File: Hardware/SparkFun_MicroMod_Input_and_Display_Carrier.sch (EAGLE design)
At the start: 64 parts, among them J1 MICROMOD-2222-C, J2 MICRO-SD, J3 USB-C_Prog, J4 AVR_SPI_PROG_3X2TESTPOINTS, J5 2.4" TFT, J6 QWIIC_RA, J7 CORTEX_JTAG_DEBUG, Q1 1.1A/60V/600mΩ, U2 ATTINY84, U5 AP7361C-33FGE

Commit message: QC Fixes
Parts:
- added TP1: TEST-POINT3, SparkFun-Connectors:TEST-POINT3
- J1: SPICEPREFIX (none) -> X
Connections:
- net SWDCK: now also TP1.1
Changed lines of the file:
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@@
 <layer number="255" name="routoute" color="7" fill="1" visible="no" active="no"/>
 </layers>
-<schematic xreflabel="%F%N/%S" xrefpart="/%S.%C%R">
+<schematic xreflabel="%F%N/%S" xrefpart="1_/%S.%C%R">
 <attributes>
 </attributes>
@@
 </classes>
 <parts>
-<part name="J1" library="SparkFun-MicroMod" deviceset="MICROMOD" device="-2222-C"/>
+<part name="J1" library="SparkFun-MicroMod" deviceset="MICROMOD" device="-2222-C">
+<attribute name="SPICEPREFIX" value="X"/>
+</part>
 <part name="J2" library="SparkFun-Connectors" deviceset="MICRO-SD-SPI" device="PUSH-PUSH" value="MICRO-SD"/>
 <part name="S1" library="SparkFun-Switches" deviceset="MOMENTARY-SWITCH-SPST" device="-SMD-5.2-TALL-REDUNDANT" value="Reset"/>
@@
 <part name="R9" library="SparkFun-Resistors" deviceset="10KOHM" device="-0603-1/10W-1%" value="10k"/>
 <part name="GND34" library="SparkFun-PowerSymbols" deviceset="GND" device=""/>
+<part name="TP1" library="SparkFun-Connectors" deviceset="TEST-POINT" device="3" value=""/>
 </parts>
 <sheets>
@@
 <attribute name="VALUE" x="15.24" y="22.606" size="1.778" layer="96" font="vector" align="top-center"/>
 </instance>
+<instance part="TP1" gate="G$1" x="185.42" y="40.64" smashed="yes">
+<attribute name="NAME" x="189.484" y="39.878" size="1.778" layer="95" font="vector"/>
+<attribute name="VALUE" x="182.88" y="38.1" size="1.778" layer="96" font="vector"/>
+</instance>
 </instances>
 <busses>
@@
 <label x="182.88" y="121.92" size="1.27" layer="95" font="vector" rot="R180" xref="yes"/>
 </segment>
-</net>
+<segment>
+<pinref part="TP1" gate="G$1" pin="1"/>
+<wire x1="185.42" y1="40.64" x2="182.88" y2="40.64" width="0.1524" layer="91"/>
+<label x="182.88" y="40.64" size="1.27" layer="95" rot="R180" xref="yes"/>
+</segment>
+</net>

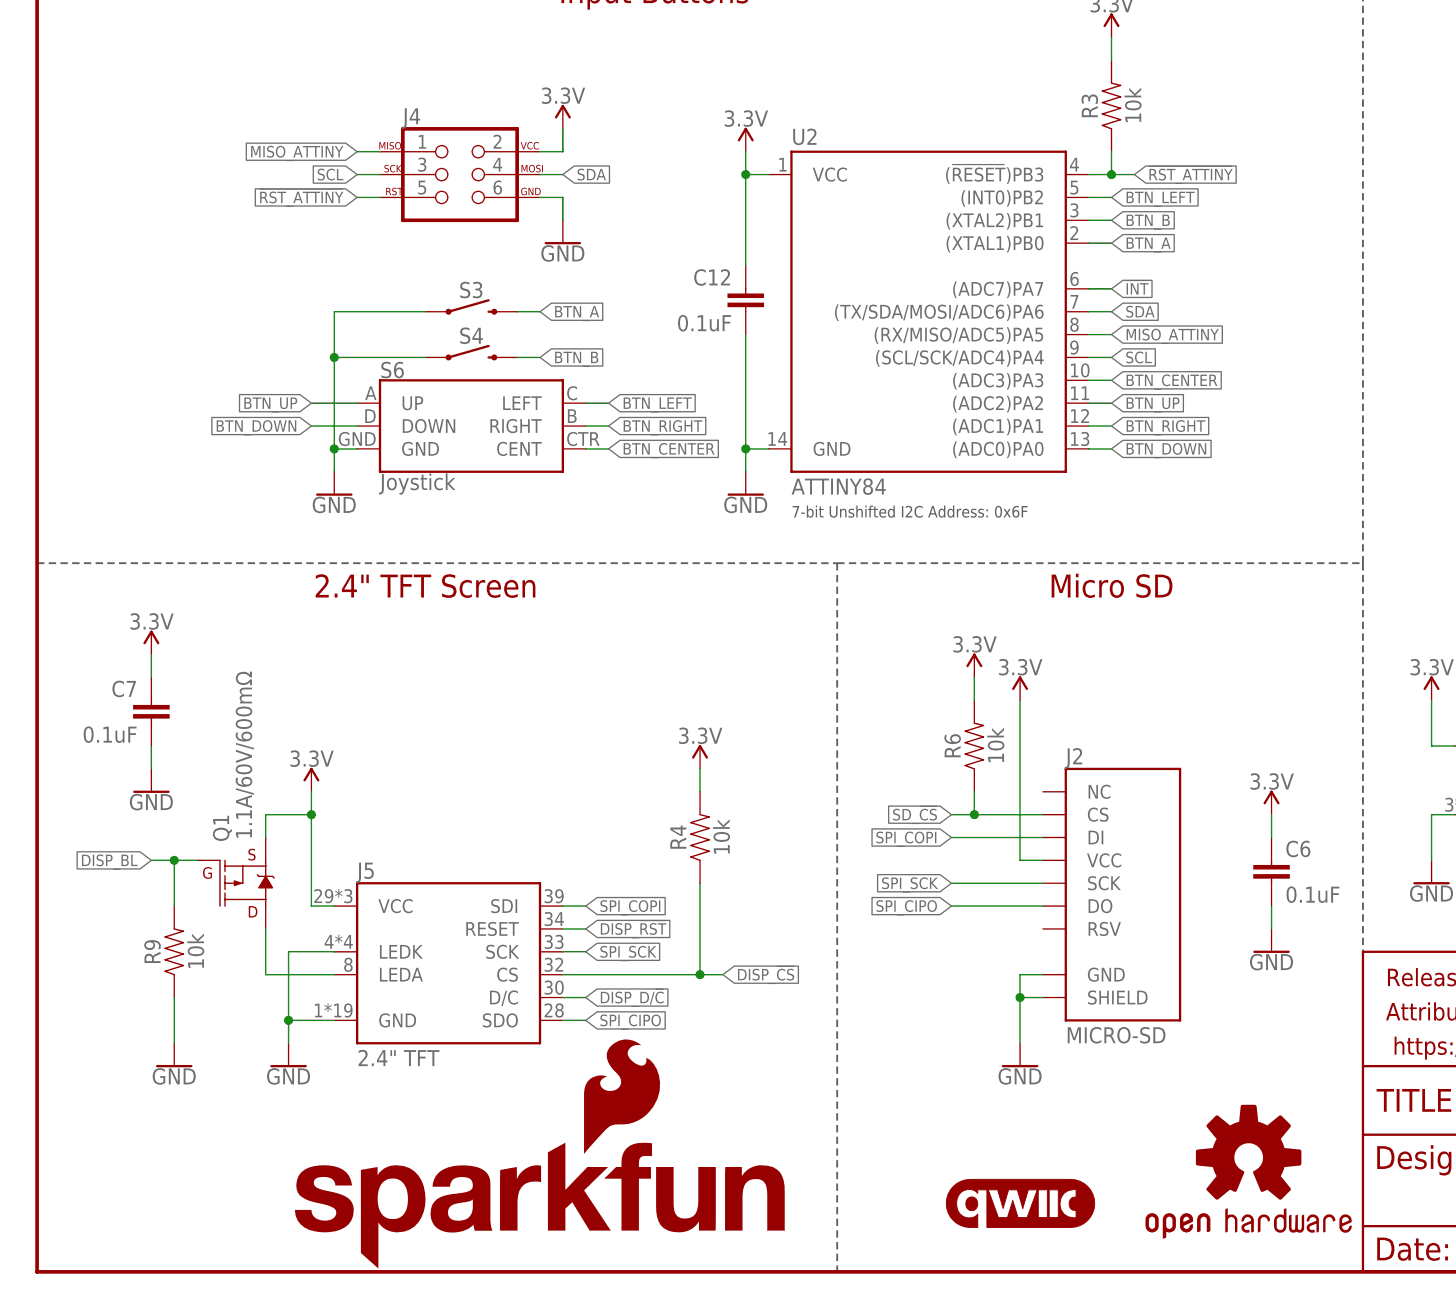
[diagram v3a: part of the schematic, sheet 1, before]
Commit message: v01 update
-Added 10ohm resistor to backlight
-Added 10k pullup to tft reset
-Connected Attiny reset to MM reset
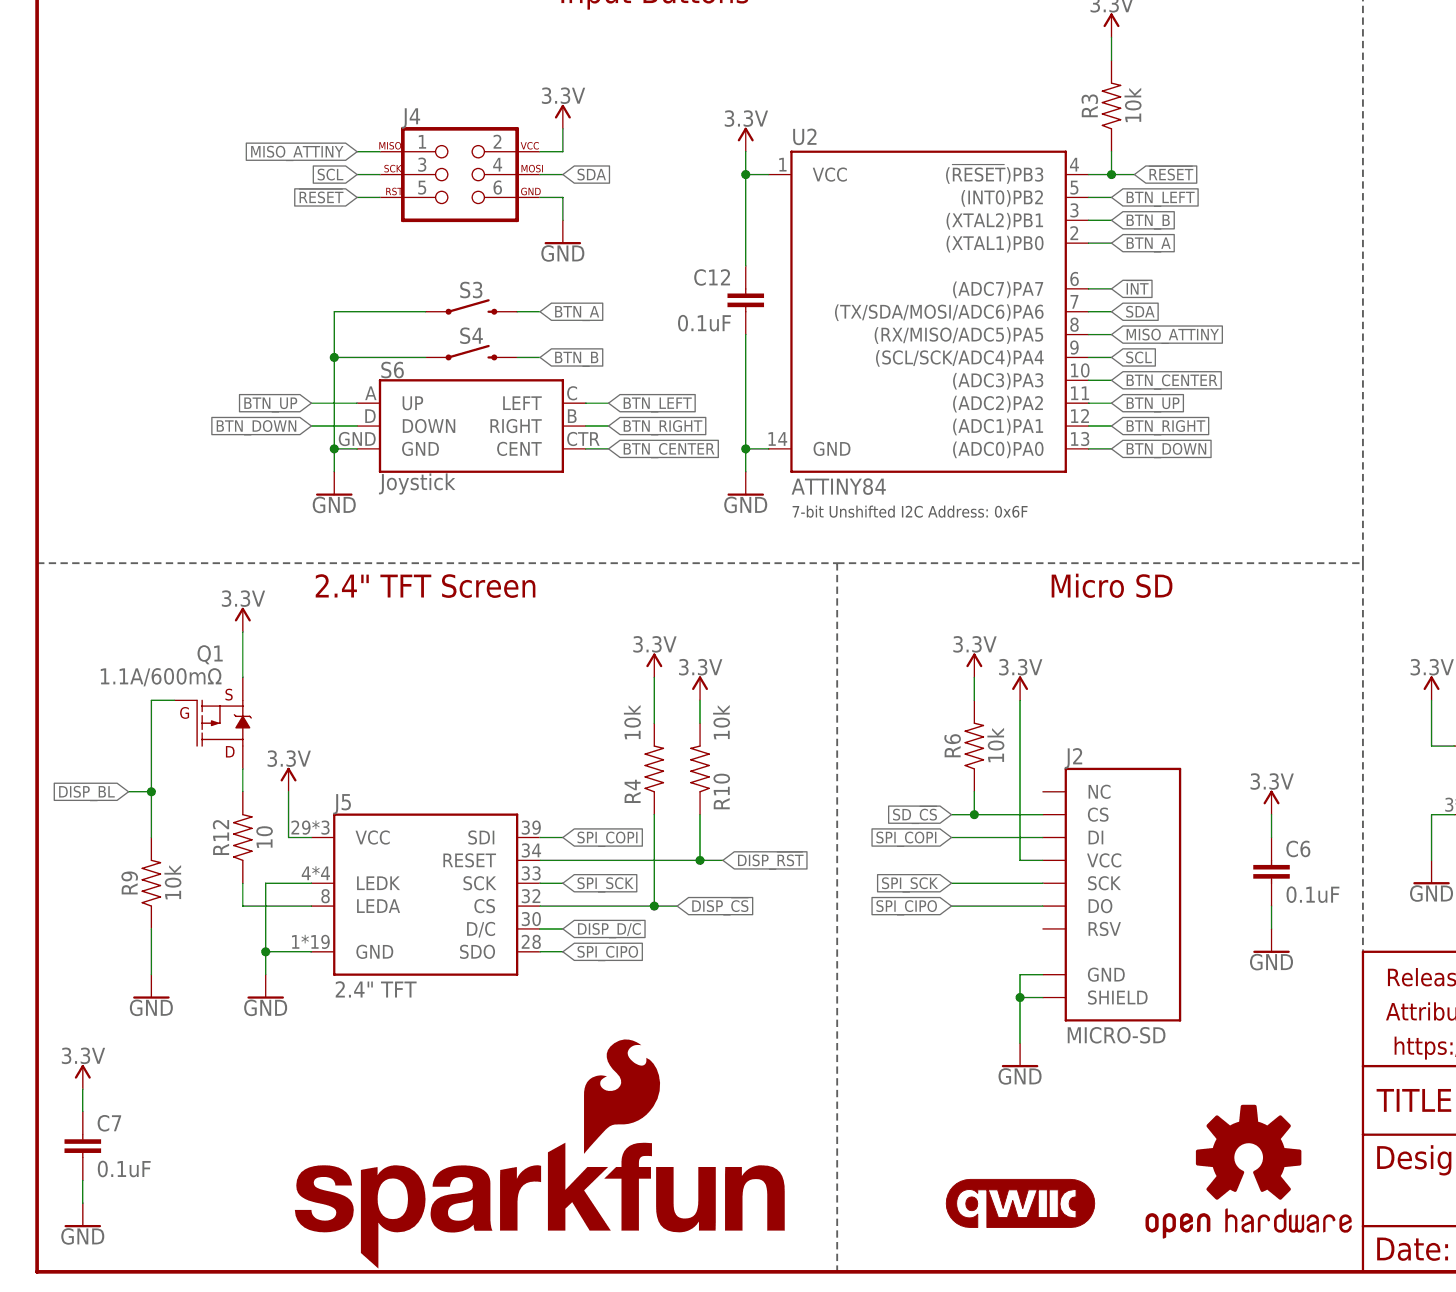
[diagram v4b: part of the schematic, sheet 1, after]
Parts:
- added R10: 10k, SparkFun-Resistors:10KOHM-0603-1/10W-1%
- added R12: 10, SparkFun-Resistors:10OHM-0603-1/10W-5%
- Q1: value 1.1A/60V/600mΩ -> 1.1A/600mΩ
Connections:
- removed net !RST_ATTINY: J4.5, R3.1, U2.(!RESET!)PB3
- removed net N$8: J5.LEDA, Q1.D
- new net N$3: J5.LEDA, R12.1
- new net N$4: Q1.D, R12.2
- net !RESET: now also J4.5, R3.1, U2.(!RESET!)PB3
- net 3.3V: now also R10.2
- net DISP_!RST: now also R10.1
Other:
- moved on the sheet: C7, J5, Q1, R4, R9

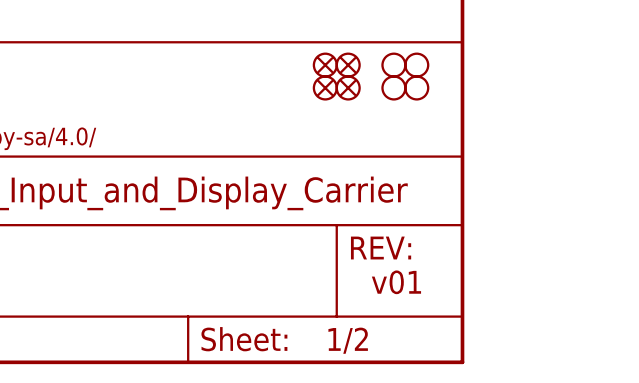
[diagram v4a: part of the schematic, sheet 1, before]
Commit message: v10
Moved display cable back slightly
Moved A and B buttons closer together
Moved measures jumper away from button A
Added silk to display outline
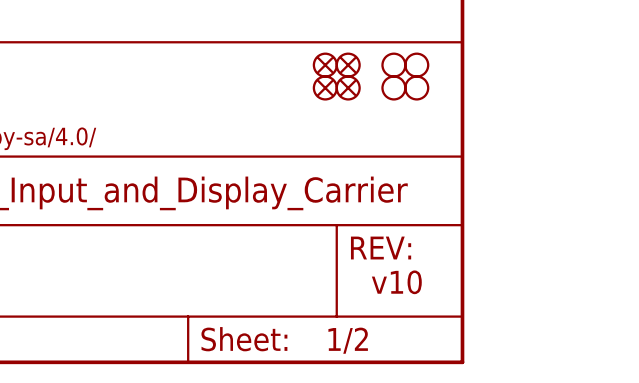
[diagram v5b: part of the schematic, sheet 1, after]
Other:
- note added: "v10"
- note removed: "v01"
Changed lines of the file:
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@@
 <?xml version="1.0" encoding="utf-8"?>
 <!DOCTYPE eagle SYSTEM "eagle.dtd">
-<eagle version="9.6.2">
+<eagle version="9.5.2">
 <drawing>
 <settings>
@@
 <layer number="255" name="routoute" color="7" fill="1" visible="no" active="no"/>
 </layers>
-<schematic xreflabel="%F%N/%S" xrefpart="1_/%S.%C%R">
+<schematic xreflabel="%F%N/%S" xrefpart="/%S.%C%R">
 <attributes>
 </attributes>
@@
 <text x="83.82" y="83.82" size="1.27" layer="97" font="vector">7-bit Unshifted I2C Address: 0x6F</text>
 <text x="165.862" y="11.43" size="2.54" layer="94" font="vector">Alex Wende</text>
-<text x="238.76" y="7.62" size="2.54" layer="94" font="vector">v01</text>
+<text x="238.76" y="7.62" size="2.54" layer="94" font="vector">v10</text>
 <wire x1="0" y1="78.74" x2="88.9" y2="78.74" width="0.2032" layer="97" style="longdash"/>
 <wire x1="88.9" y1="78.74" x2="147.32" y2="78.74" width="0.2032" layer="97" style="longdash"/>

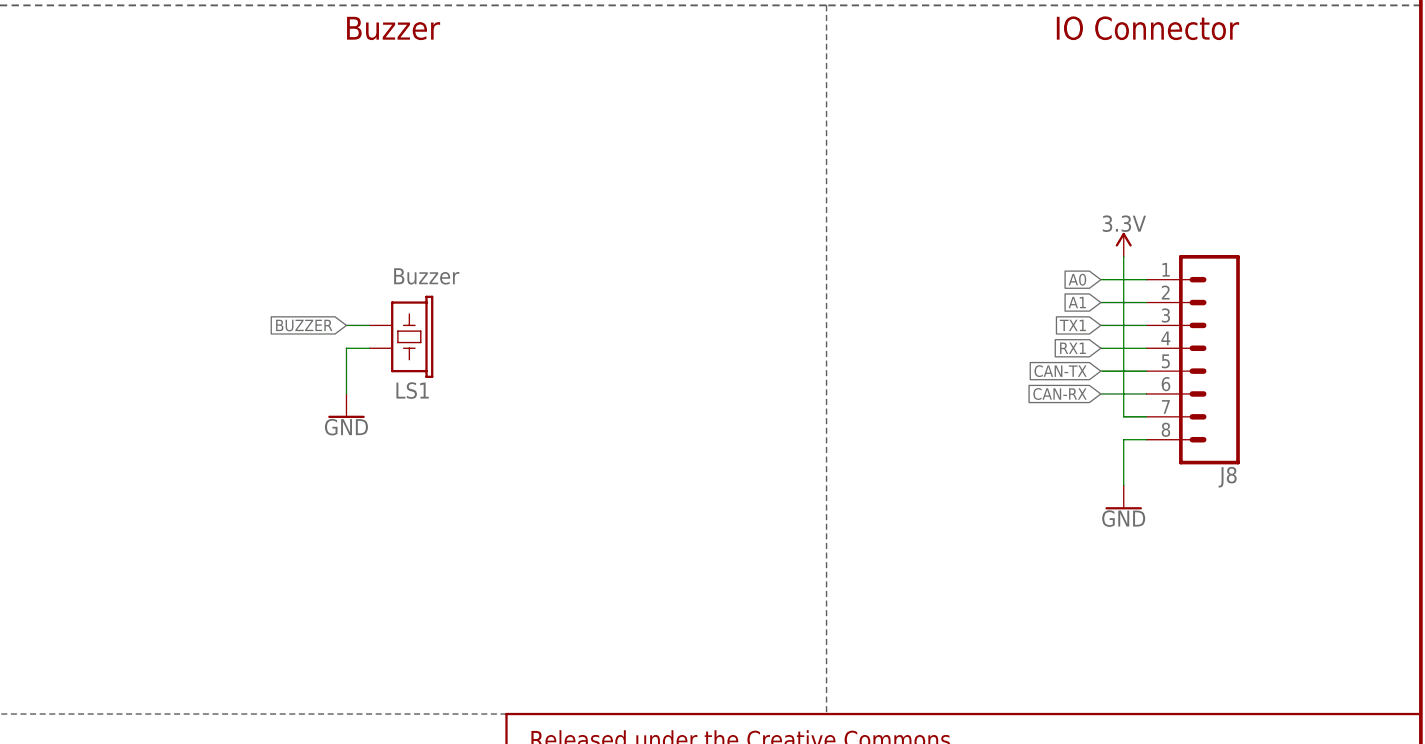
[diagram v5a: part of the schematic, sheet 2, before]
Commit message: v10 post review changes
-Added 5V/V_USB pin
-Added BJT to buzzer
-Replaced pull up/down resistors from 10lk to 100k
-Replaced 1/10W 10ohm resistor with 1/4W 10ohm
-Removed display outline on tPlace layer
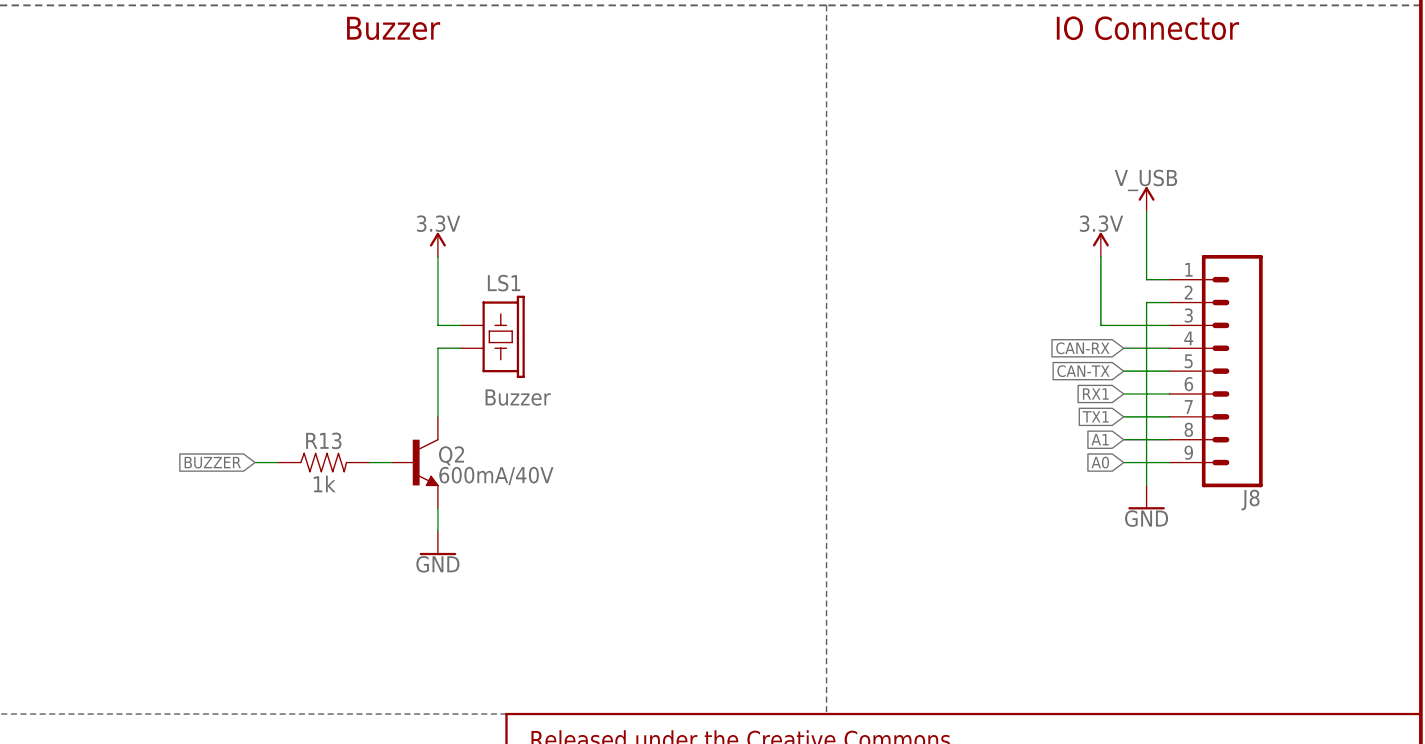
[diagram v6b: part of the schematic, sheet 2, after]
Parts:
- added Q2: 600mA/40V, SparkFun-DiscreteSemi:TRANS_NPN-MMBT2222AL
- added R13: 1k, SparkFun-Resistors:1KOHM-0603-1/10W-1%
- J8: device SparkFun-Connectors:CONN_08NO_SILK_DNP -> SparkFun-Connectors:CONN_09NO_SILK
- R10, R3, R4, R6, R9: value 10k -> 100k; device SparkFun-Resistors:10KOHM-0603-1/10W-1% -> SparkFun-Resistors:100KOHM-0603-1/10W-1%
- R12: device SparkFun-Resistors:10OHM-0603-1/10W-5% -> SparkFun-Resistors:10OHM-1206-1/4W-1%
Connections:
- new net N$5: LS1.2, Q2.C
- new net N$6: Q2.B, R13.2
- net 3.3V: now also J8.3, LS1.1; no longer J8.7
- net A0: now also J8.9; no longer J8.1
- net A1: now also J8.8; no longer J8.2
- net BUZZER: now also R13.1; no longer LS1.2
- net CAN-RX: now also J8.4; no longer J8.6
- net GND: now also J8.2, Q2.E; no longer J8.8, LS1.1
- net RX1: now also J8.6; no longer J8.4
- net TX1: now also J8.7; no longer J8.3
- net V_USB: now also J8.1
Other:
- moved on the sheet: LS1
